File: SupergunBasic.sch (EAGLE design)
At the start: 33 parts, among them J1 AUDIO_JACK_3.5MM_PTH

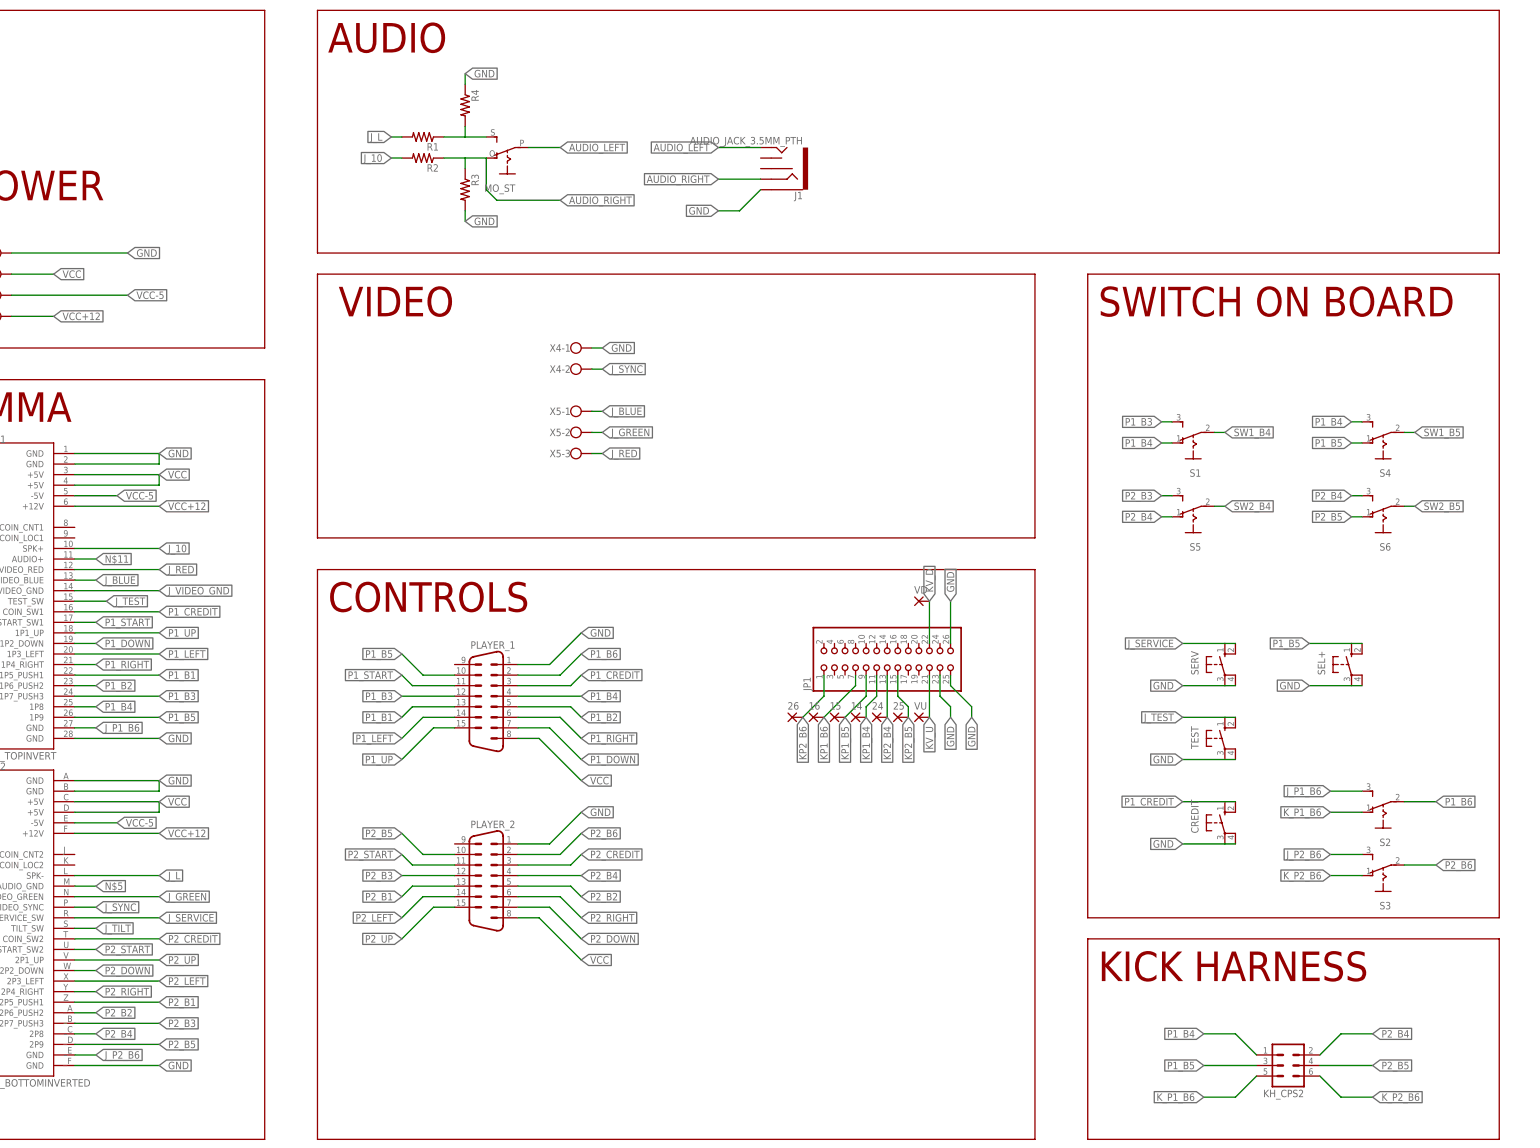
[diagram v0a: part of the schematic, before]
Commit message: Add files via upload
He estado trabajando en la versión con Scart, es mas fácil quitar que añadir cosas, así que en el momento de subir esta versión, es identica a la Scart pero sin los requisitos de este.
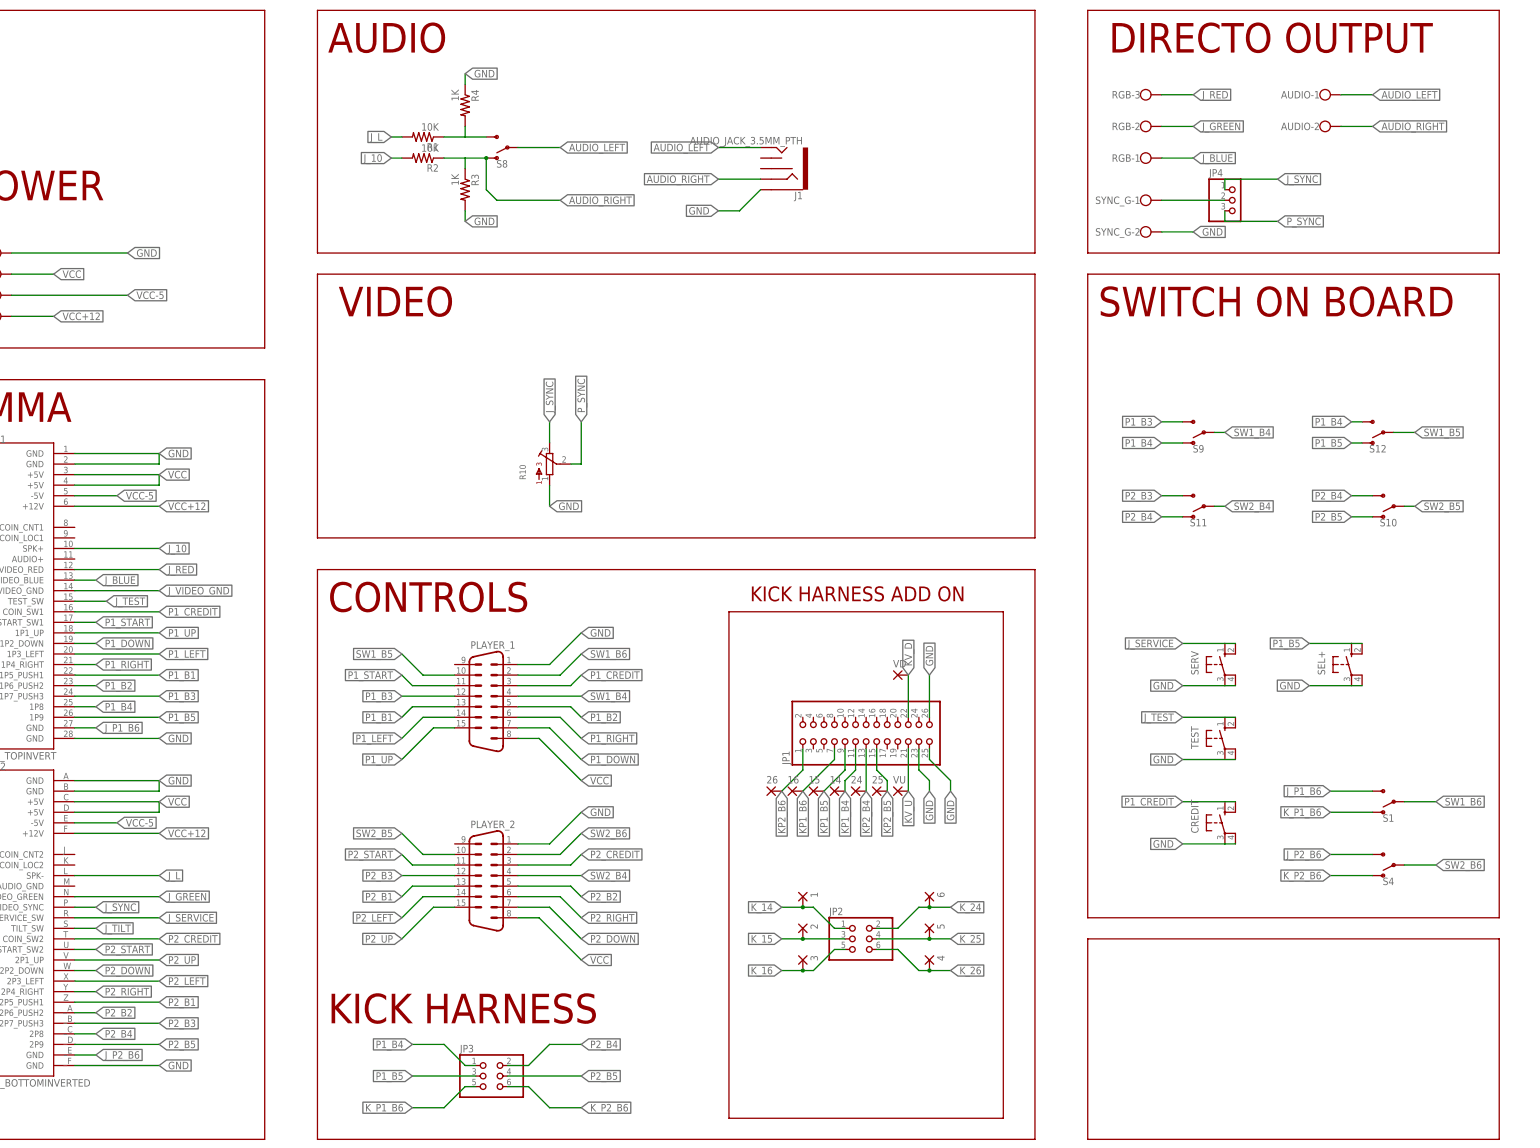
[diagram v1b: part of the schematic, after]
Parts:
- removed KH_CPS2: (no value), con-lstb:MA03-2
- removed MO_ST: (no value), adafruit:EG1218S
- removed S2, S3, S5, S6: (no value), switch:255SB
- removed X4: (no value), con-wago-500:W237-102
- removed X5: (no value), con-wago-500:W237-103
- added 1, 2, 3, 4, 5, 6: (no value), wirepad:SMD2
- added AUDIO, SYNC_G: (no value), con-wago-500:W237-102
- added JP2, JP3: (no value), pinhead:PINHD-2X3
- added JP4: (no value), pinhead:PINHD-1X3
- added R10: (no value), bourns:3362P
- added RGB: (no value), con-wago-500:W237-103
- added S10, S11, S12, S8, S9: (no value), SparkFun-Switches:SWITCH-SPDT-PTH-11.6X4.0MM
- R1, R2: value (none) -> 10K
- R3, R4: value (none) -> 1K
- S1, S4: device switch:255SB -> SparkFun-Switches:SWITCH-SPDT-PTH-11.6X4.0MM
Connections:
- removed net N$11: JAMMA1.AUDIO+
- removed net N$3: MO_ST.S, R1.1, R4.2
- removed net N$5: JAMMA2.AUDIO_GND
- removed net P1_B6: PLAYER_1.2, S2.P
- removed net P2_B6: PLAYER_2.2, S3.P
- new net DIRECT_SYNC: JP4.2, SYNC_G-1.KL
- new net K_14: 1.P, JP2.1
- new net K_15: 2.P, JP2.3
- new net K_16: 3.P, JP2.5
- new net K_24: 6.P, JP2.2
- new net K_25: 5.P, JP2.4
- new net K_26: 4.P, JP2.6
- new net P_SYNC: JP4.3, R10.2
- new net STR_LEFT: R1.1, R4.2, S8.S
- new net SW1_B6: PLAYER_1.2, S1.P
- new net SW2_B6: PLAYER_2.2, S4.P
- net AUDIO_LEFT: now also AUDIO-1.KL, S8.P; no longer MO_ST.P
- net AUDIO_RIGHT: now also AUDIO-2.KL, S8.O; no longer MO_ST.O
- net GND: now also R10.1, SYNC_G-2.KL; no longer X4-1.KL
- net J_BLUE: now also RGB-1.KL; no longer X5-1.KL
- net J_GREEN: now also RGB-2.KL; no longer X5-2.KL
- net J_P1_B6: now also S1.S; no longer S2.S
- net J_P2_B6: now also S4.S; no longer S3.S
- net J_RED: now also RGB-3.KL; no longer X5-3.KL
- net J_SYNC: now also JP4.1, R10.3; no longer X4-2.KL
- net K_P1_B6: now also JP3.5, S1.O; no longer KH_CPS2.5, S2.O
- net K_P2_B6: now also JP3.6, S4.O; no longer KH_CPS2.6, S3.O
- net P1_B3: now also S9.S; no longer S1.S
- net P1_B4: now also JP3.1, S12.S, S9.O; no longer KH_CPS2.1, PLAYER_1.4, S1.O, S4.S
- net P1_B5: now also JP3.3, S12.O; no longer KH_CPS2.3, PLAYER_1.10, S4.O
- net P2_B3: now also S11.S; no longer S5.S
- net P2_B4: now also JP3.2, S10.S, S11.O; no longer KH_CPS2.2, PLAYER_2.4, S5.O, S6.S
- net P2_B5: now also JP3.4, S10.O; no longer KH_CPS2.4, PLAYER_2.10, S6.O
- net SW1_B4: now also PLAYER_1.4, S9.P; no longer S1.P
- net SW1_B5: now also PLAYER_1.10, S12.P; no longer S4.P
- net SW2_B4: now also PLAYER_2.4, S11.P; no longer S5.P
- net SW2_B5: now also PLAYER_2.10, S10.P; no longer S6.P
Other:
- note added: "DIRECTO OUTPUT"
- note added: "KICK HARNESS ADD ON"
- moved on the sheet: 14, 15, 16, 24, 25, 26, JP1, VD, VU

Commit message: Add files via upload
There ara some changesr since las versión, now there's a lm1881 sync stripper to get Sync On Green to Scart Connector. But if you are using a OSSC theres a switch to select Jamma Sync (original) or Csync (LM1881)

Now there's a LED to bring light to the PCB!

Minir improvements on design
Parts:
- added C1, C2: 0.1uF, SparkFun-Capacitors:0.1UF-KIT-EZ-50V-20%
- added IC1: LM1881N, oldchips2:LM1881N
- added JP5: (no value), pinhead:PINHD-1X3
- added LED1: (no value), led:LEDLD260
- added R11: 680k, adafruit:R-US_0204/7
- added R5, R6, R7: (no value), bourns:3362P
- added R8: 220, adafruit:R-US_0204/7
- added R9: 560, adafruit:R-US_0204/7
- added U$1: SCART_F, scart:SCART_F
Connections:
- new net A_LEFT_OUT: J1.TSH, U$1.3
- new net A_RIGHT_OUT: J1.RSH, U$1.1
- new net C_SYNC: IC1G$1.CSYNC, JP5.3
- new net N$2: LED1.A, R8.2
- new net N$4: C2.1, IC1G$1.RSET, R11.2
- new net N$5: C1.2, IC1G$1.VIDEO
- new net SCART_FAST_SW: R9.2, U$1.16
- new net SCART_SYNC: JP5.2, U$1.19
- new net S_BLUE: R7.2, U$1.7
- new net S_GREEN: R6.2, U$1.11
- new net S_RED: R5.2, U$1.15
- new net VSYNC: IC1G$1.VS
- net GND: now also C2.2, IC1P.GND, LED1.C, R11.1, R5.1, R6.1, R7.1, U$1.13, U$1.14, U$1.17, U$1.18, U$1.21, U$1.4, U$1.5, U$1.9
- net J_BLUE: now also R7.3
- net J_GREEN: now also C1.1, R6.3
- net J_RED: now also R5.3
- net J_SYNC: now also JP5.1
- net VCC: now also IC1P.VCC, R8.1
- net VCC+12: now also R9.1, U$1.8
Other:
- note added: "DIRECT OUTPUT"
- note added: "SYNC ON GREEN"
- note removed: "DIRECTO OUTPUT"
